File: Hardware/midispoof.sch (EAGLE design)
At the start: 21 parts, among them IC1 7805L, J1 DCJ0202, J2 STEREOSWS, M1 ARDUINO-NANO-3.0#ISP, U1 MICROCHIP_MCP41010-I-PMICROCH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

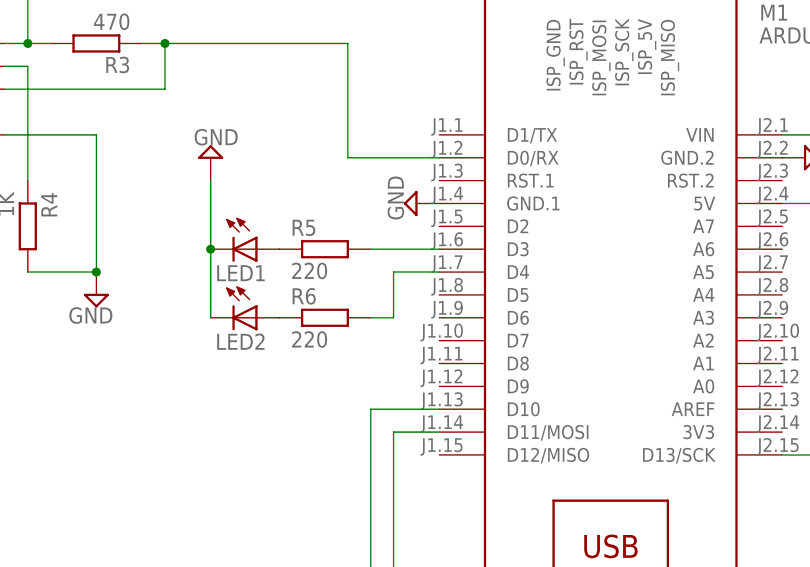
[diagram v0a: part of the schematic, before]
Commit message: Corrected missing supply flood fills on PCB layout
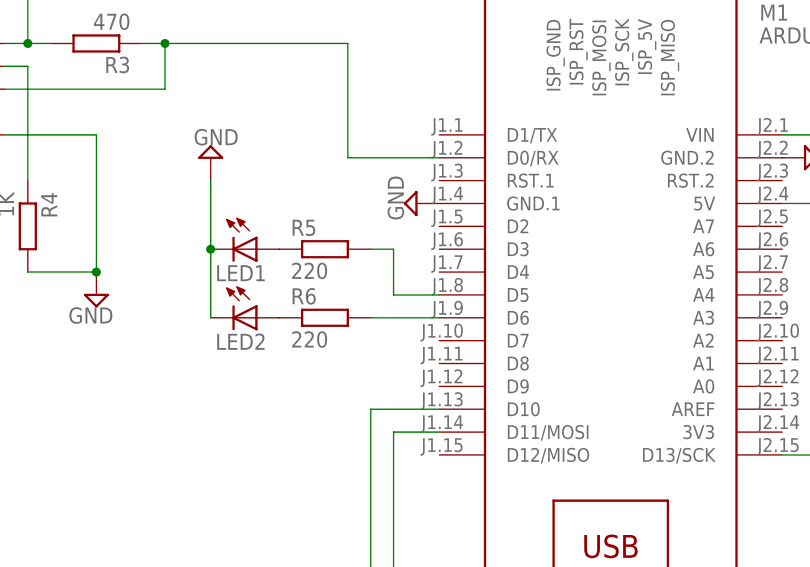
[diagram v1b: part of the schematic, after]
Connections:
- net N$18: now also M1.D5; no longer M1.D3
- net N$19: now also M1.D6; no longer M1.D4
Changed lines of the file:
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@@
 <net name="N$18" class="0">
 <segment>
-<pinref part="M1" gate="G$1" pin="D3"/>
 <pinref part="R5" gate="G$1" pin="2"/>
-<wire x1="167.64" y1="121.92" x2="160.02" y2="121.92" width="0.1524" layer="91"/>
+<wire x1="162.56" y1="121.92" x2="160.02" y2="121.92" width="0.1524" layer="91"/>
+<wire x1="162.56" y1="121.92" x2="162.56" y2="116.84" width="0.1524" layer="91"/>
+<pinref part="M1" gate="G$1" pin="D5"/>
+<wire x1="162.56" y1="116.84" x2="167.64" y2="116.84" width="0.1524" layer="91"/>
 </segment>
 </net>
 <net name="N$19" class="0">
 <segment>
-<pinref part="M1" gate="G$1" pin="D4"/>
-<wire x1="167.64" y1="119.38" x2="162.56" y2="119.38" width="0.1524" layer="91"/>
-<wire x1="162.56" y1="119.38" x2="162.56" y2="114.3" width="0.1524" layer="91"/>
 <pinref part="R6" gate="G$1" pin="2"/>
-<wire x1="162.56" y1="114.3" x2="160.02" y2="114.3" width="0.1524" layer="91"/>
+<pinref part="M1" gate="G$1" pin="D6"/>
+<wire x1="160.02" y1="114.3" x2="167.64" y2="114.3" width="0.1524" layer="91"/>
 </segment>
 </net>
